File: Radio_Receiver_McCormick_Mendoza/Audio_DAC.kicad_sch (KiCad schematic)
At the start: 46 parts, among them J35 3.5mm_Jack, J38 DAC_FLT, J40 DAC_FMT, J46 3.5mm_Jack, U14 PCM5102A

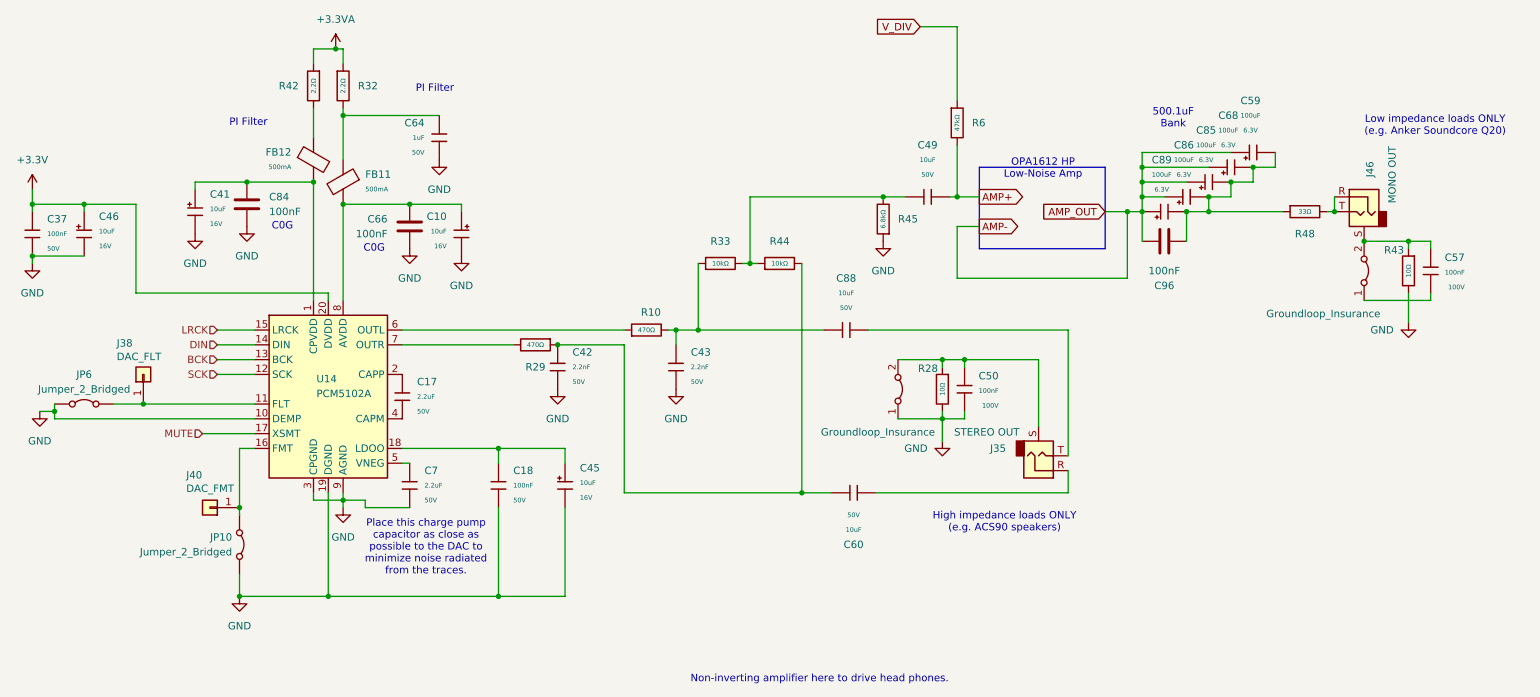
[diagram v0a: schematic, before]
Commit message: Routed antenna and isolated GNDA
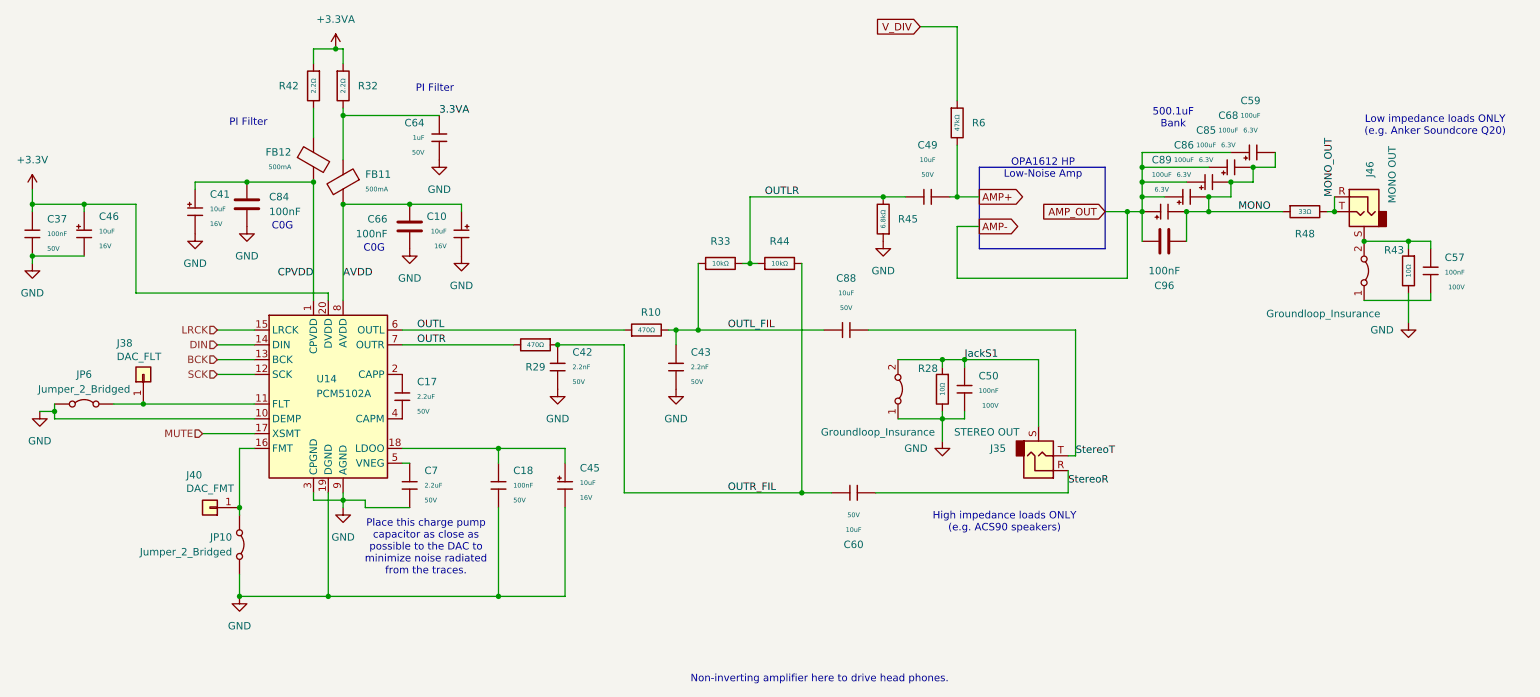
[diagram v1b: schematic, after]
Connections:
- net 3.3VA: now reaches C64.1, FB11.1, R32.2
- net OUTLR: now reaches C49.1, R33.2, R44.1, R45.2
- net OUTR_FIL: now reaches C42.1, C60.1, R29.1, R44.2
- net CPVDD: now reaches C41.1, C84.1, FB12.2, U14.1 (CPVDD)
- net MONO: now reaches C59.2, C68.2, C85.2, C86.2, C89.2, C96.2, R48.1
- net OUTL: now reaches R10.1, U14.6 (OUTL)
- net OUTL_FIL: now reaches C43.1, C88.2, R10.2, R33.1
- net MONO_OUT: now reaches J46.R, J46.T, R48.2
- net OUTR: now reaches R29.2, U14.7 (OUTR)
- net AVDD: now reaches C10.1, C66.1, FB11.2, U14.8 (AVDD)
- net StereoR: now reaches C60.2, J35.R
- net JackS1: now reaches C50.2, J35.S, R28.1, e3.2 (B)
- net StereoT: now reaches C88.1, J35.T
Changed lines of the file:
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@@
-	(wire
-		(pts
-			(xy 167.64 96.52) (xy 201.93 96.52)
-		)
-		(stroke
-			(width 0)
-			(type default)
-		)
-	)
 	(wire
 		(pts
@@
 	(wire
 		(pts
+			(xy 203.2 96.52) (xy 167.64 96.52)
+		)
+		(stroke
+			(width 0)
+			(type default)
+		)
+	)
+	(wire
+		(pts
 			(xy 24.13 74.93) (xy 33.02 74.93)
 		)
@@
 	(wire
 		(pts
+			(xy 203.2 118.11) (xy 203.2 96.52)
+		)
+		(stroke
+			(width 0)
+			(type default)
+		)
+	)
+	(wire
+		(pts
 			(xy 104.14 142.24) (xy 74.93 142.24)
 		)
@@
 	(wire
 		(pts
+			(xy 203.2 118.11) (xy 201.93 118.11)
+		)
+		(stroke
+			(width 0)
+			(type default)
+		)
+	)
+	(wire
+		(pts
 			(xy 24.13 72.39) (xy 24.13 74.93)
 		)
@@
 	(wire
 		(pts
-			(xy 77.47 91.44) (xy 77.47 74.93)
+			(xy 77.47 74.93) (xy 77.47 91.44)
 		)
 		(stroke
@@
 		)
 	)
-	(wire
-		(pts
-			(xy 201.93 118.11) (xy 201.93 96.52)
-		)
-		(stroke
-			(width 0)
-			(type default)
-		)
-	)
 	(polyline
 		(pts
@@
 		)
 	)
+	(label "3.3VA"
+		(at 93.98 59.69 0)
+		(effects
+			(font
+				(size 1.27 1.27)
+			)
+			(justify left bottom)
+		)
+	)
+	(label "OUTR_FIL"
+		(at 143.51 124.46 0)
+		(effects
+			(font
+				(size 1.27 1.27)
+			)
+			(justify left bottom)
+		)
+	)
+	(label "OUTL_FIL"
+		(at 143.51 96.52 0)
+		(effects
+			(font
+				(size 1.27 1.27)
+			)
+			(justify left bottom)
+		)
+	)
+	(label "MONO"
+		(at 231.14 76.2 0)
+		(effects
+			(font
+				(size 1.27 1.27)
+			)
+			(justify left bottom)
+		)
+	)
+	(label "CPVDD"
+		(at 72.39 87.63 180)
+		(effects
+			(font
+				(size 1.27 1.27)
+			)
+			(justify right bottom)
+		)
+	)
+	(label "OUTR"
+		(at 90.17 99.06 0)
+		(effects
+			(font
+				(size 1.27 1.27)
+			)
+			(justify left bottom)
+		)
+	)
+	(label "MONO_OUT"
+		(at 247.65 73.66 90)
+		(effects
+			(font
+				(size 1.27 1.27)
+			)
+			(justify left bottom)
+		)
+	)
+	(label "StereoT"
+		(at 203.2 118.11 0)
+		(effects
+			(font
+				(size 1.27 1.27)
+			)
+			(justify left bottom)
+		)
+	)
+	(label "JackS1"
+		(at 184.15 101.6 0)
+		(effects
+			(font
+				(size 1.27 1.27)
+			)
+			(justify left bottom)
+		)
+	)
+	(label "StereoR"
+		(at 201.93 123.19 0)
+		(effects
+			(font
+				(size 1.27 1.27)
+			)
+			(justify left bottom)
+		)
+	)
+	(label "OUTLR"
+		(at 149.86 73.66 0)
+		(effects
+			(font
+				(size 1.27 1.27)
+			)
+			(justify left bottom)
+		)
+	)
+	(label "OUTL"
+		(at 90.17 96.52 0)
+		(effects
+			(font
+				(size 1.27 1.27)
+			)
+			(justify left bottom)
+		)
+	)
+	(label "AVDD"
+		(at 77.47 87.63 0)
+		(effects
+			(font
+				(size 1.27 1.27)
+			)
+			(justify left bottom)
+		)
+	)

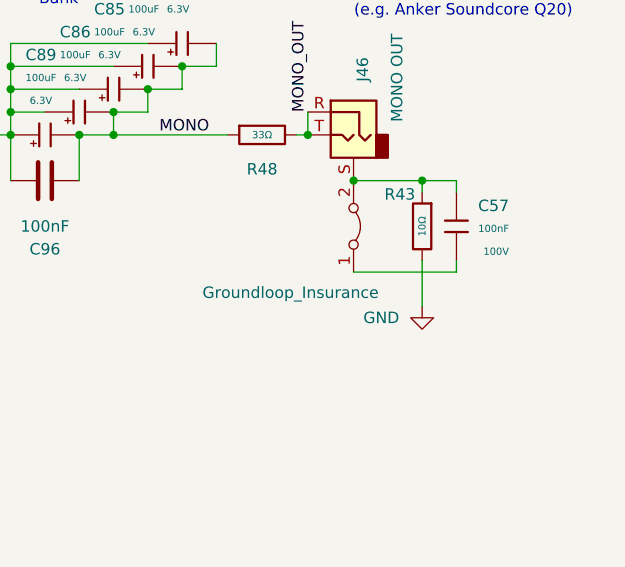
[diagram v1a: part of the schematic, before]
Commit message: Finished routing master copy and added GND and PWR planes with vias
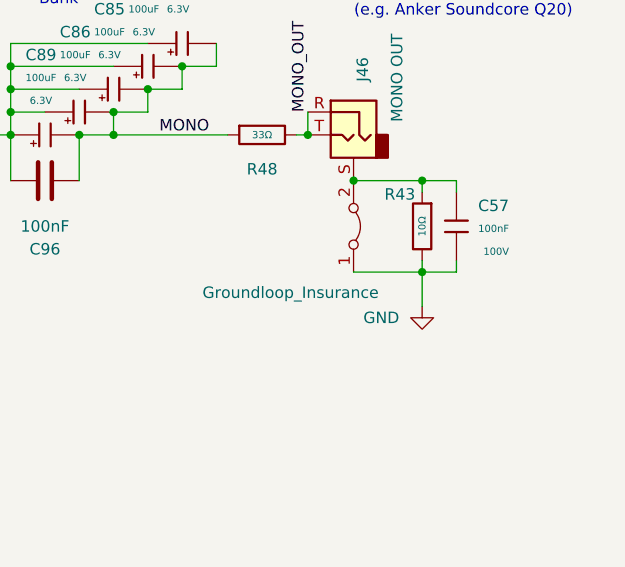
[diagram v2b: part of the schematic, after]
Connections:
- net GND: now also C57.1, e4.1 (A)
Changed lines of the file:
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@@
+	)
+	(junction
+		(at 260.35 91.44)
+		(diameter 0)
+		(color 0 0 0 0)
 	)
 	(junction
@@
 	(wire
 		(pts
+			(xy 260.35 91.44) (xy 260.35 95.25)
+		)
+		(stroke
+			(width 0)
+			(type default)
+		)
+	)
+	(wire
+		(pts
 			(xy 264.16 81.28) (xy 260.35 81.28)
 		)
@@
 	(wire
 		(pts
-			(xy 264.16 91.44) (xy 252.73 91.44)
+			(xy 264.16 91.44) (xy 260.35 91.44)
 		)
 		(stroke
@@
 	(wire
 		(pts
-			(xy 260.35 90.17) (xy 260.35 95.25)
+			(xy 260.35 90.17) (xy 260.35 91.44)
 		)
 		(stroke
@@
 		)
 		(stroke
+			(width 0)
+			(type default)
+		)
+	)
+	(wire
+		(pts
+			(xy 260.35 91.44) (xy 252.73 91.44)
+		)
+		(stroke

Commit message: Corrected stereo and mono audio jacks' footprints
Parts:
- J35, J46: footprint Connector_Audio:Jack_3.5mm_CUI_SJ-3523-SMT_Horizontal -> Reciever_Parts:Jack_3.5mm_CUI_SJ-3523-SMT_Horizontal
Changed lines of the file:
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@@
 			)
 		)
-		(property "Footprint" "Connector_Audio:Jack_3.5mm_CUI_SJ-3523-SMT_Horizontal"
+		(property "Footprint" "Reciever_Parts:Jack_3.5mm_CUI_SJ-3523-SMT_Horizontal"
 			(at 252.73 76.2 0)
 			(hide yes)
@@
 			)
 		)
-		(property "Footprint" "Connector_Audio:Jack_3.5mm_CUI_SJ-3523-SMT_Horizontal"
+		(property "Footprint" "Reciever_Parts:Jack_3.5mm_CUI_SJ-3523-SMT_Horizontal"
 			(at 196.85 118.11 0)
 			(hide yes)
